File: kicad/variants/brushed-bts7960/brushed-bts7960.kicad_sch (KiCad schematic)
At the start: 57 parts, among them IC1 rp2040_RP2040_breakout_swd, J1 HDR-M-2.54_1x3, J2 HDR-M-2.54_1x4, J3 HDR-M-2.54_1x4, J4 HDR-M-2.54_1x4, U1 SN74AHC244DW, U2 BTN7970, U3 BTN7970, U4 BTN7970, U5 BTN7970, U6 BMI160, U7 SPX3819M5-L-3-3/TR

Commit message: feat(kicad): импорт платы из EasyEDA в KiCad
Завершает перенос варианта brushed-bts7960: схема уже была, плата
оставалась только в исходнике EasyEDA (easyeda/RP2040/PCB_RP2040.json).

Плату импортирует штатный конвертер KiCad (kicad-cli pcb import, формат
EasyEDA / JLCEDA Std) — свой парсер не пишем. Новый scripts/gen_pcb.py
поверх него доводит результат до вида репозитория:

- правила DRC из DRCRULE исходника (зазор 0.152 мм, дорожка 0.254 мм,
  via 0.61/0.305 мм, отдельный класс 5v) — иначе плата остаётся с
  дефолтами KiCad, под которые она не разводилась;
- перезаливка полигонов штатным ZONE_FILLER: импортёр переносит контуры
  COPPERAREA без вырезов под чужие цепи (~900 ложных нарушений DRC);
- выгрузка 14 футпринтов в kicad/common/footprints/biba.pretty/,
  канонические имена слоёв вместо EasyEDA-псевдонимов;
- 425 свободных падов и отверстий помечены board-only.

Схема и плата связаны: easyeda_sch2kicad.py проставляет Footprint,
имена у обоих генераторов из общей easyeda_netlist.footprint_name().

Проверено: связность совпадает с исходником побитово (56 сетей,
220 пин-назначений), 0 неразведённых пар, гербера и сверловка
экспортируются. DRC 1501 -> 555, остаток — свойства исходника
(массивы via в courtyard, шелкография, пады 0805/0603 без паяльной
пасты), разобран в README варианта.

gen_schematic.py помечен устаревшим (его вытеснил easyeda_sch2kicad.py)
и больше не затирает fp-lib-table и .kicad_pro.

Co-Authored-By: Claude Opus 5 <noreply@anthropic.com>
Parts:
- C1, C2, C3, C4, C5, C6: footprint (none) -> biba:C0805
- C7, C8: footprint (none) -> biba:C0603
- C9: footprint (none) -> biba:CAP-TH_BD16.0-P7.50-D0.8-FD-H25.0
- H1, H10, H2, H3, H4, H5, H6, H7, H8: footprint (none) -> biba:HDR-F-2.54_1X3
- IC1: footprint (none) -> biba:RP2040-BREAKOUT_SWD
- J1: footprint (none) -> biba:HDR-M-2.54_1X3
- J2, J3, J4: footprint (none) -> biba:HDR-M-2.54_1X4
- PM1: footprint (none) -> biba:SKMW30G-05
- R1, R10, R11, R12, R13, R14, R15, R16, R17, R18, R19, R2, R20, R25, R26, R3, R4, R5, R6, R7, R8, R9: footprint (none) -> biba:R0805
- R21, R22, R23, R24: footprint (none) -> biba:R0603
- U1: footprint (none) -> biba:SOIC-20_L12.8-W7.5-P1.27-LS10.3-BL
- U2, U3, U4, U5: footprint (none) -> biba:TO-263-7_L10.2-W10.4-P1.27-LS14.4-B
- U6: footprint (none) -> biba:LGA-14_L3.0-W2.5-P0.50-BL
- U7: footprint (none) -> biba:SOT-23-5_L3.0-W1.7-P0.95-LS2.8-BR

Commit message: feat(kicad): снабберы, супрессоры и керамика по питанию драйверов
Доработка по analysis/M1-driver-failure.md §5 — то, чего на плате не
хватало и что разбиралось при отказе нижнего ключа U2.

Добавлено в схему (11 позиций, стало 68 компонентов / 58 цепей):

- C10-C13 470 нФ X7R 50 В — керамика VS-GND у каждого драйвера U2-U5
  (§5.1); раньше её не было ни у одного.
- C14 1000 мкФ 50 В low-ESR — DC-link у пары U2/U3 (§5.2); единственный
  C9 стоит у U5, до U2/U3 по шине VIN 50-80 мм.
- R27+C15, R28+C16 — RC-снабберы 22 Ом 5 Вт + 100 нФ 100 В плёнка между
  выходами каждого моста, M1+/M1- и M2+/M2- (§5.7). 22 Ом — верх
  диапазона 10-22 Ом; рассеивание P=C*V^2*f ~1.3-2.5 Вт от R не зависит,
  а пиковый ток на фронте 1.1 А против 2.5 А при 10 Ом.
- D1, D2 1.5KE30CA — двунаправленные супрессоры на выводах моторов,
  параллельно снабберам. У 1.5KE30CA VC=41.4 В при 36 А, ниже
  абсолютного максимума VS=45 В у BTN7970.

Шина VIN осталась без супрессора: §5.3 анализа и статья держат TVS
именно там. Закрывается третьим корпусом D3 на VIN-GND у клеммы.

Заведён символ biba:TVS_BIDIR; футпринты выводных деталей — из
стандартных библиотек KiCad, резолвятся через глобальную fp-lib-table.

Метка цепи Vin -> VIN: имена сетей в KiCad регистрозависимы, на плате и
во всей документации цепь называется VIN.

Оба конвертера EasyEDA теперь отказываются затирать существующие
.kicad_sch/.kicad_pcb без --force: импорт разовый, дальше проект
ведётся в KiCad.

ERC без новых замечаний (остаются 2 исходные power_pin_not_driven).
На плату не перенесено.

Co-Authored-By: Claude Opus 5 <noreply@anthropic.com>
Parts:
- added C10, C11, C12, C13: 470n, biba:C0805, symbol biba:C
- added C14: 1000u, biba:CAP-TH_BD16.0-P7.50-D0.8-FD-H25.0, symbol biba:C_Pol
- added C15, C16: 100n 100V, Capacitor_THT:C_Rect_L10.0mm_W5.0mm_P5.00mm_P7.50mm, symbol biba:C
- added D1, D2: 1.5KE30CA, Diode_THT:D_DO-201AE_P15.24mm_Horizontal, symbol biba:TVS_BIDIR
- added R27, R28: 22R 5W, Resistor_THT:R_Axial_Power_L25.0mm_W9.0mm_P30.48mm, symbol biba:R
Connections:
- net GND: now also C10.2, C11.2, C12.2, C13.2, C14.2
- net M1+: now also D1.1 (A1), R27.1
- net M1-: now also C15.2, D1.2 (A2)
- net M2+: now also D2.1 (A1), R28.1
- net M2-: now also C16.2, D2.2 (A2)
- net Vin renamed VIN
- net VIN: now also C10.1, C11.1, C12.1, C13.1, C14.1
- new net M1_SNUB: C15.1, R27.2
- new net M2_SNUB: C16.1, R28.2
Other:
- note added: "50V low-ESR, у пары U2/U3"
- note added: "X7R 50V, VS-GND у U2"
- note added: "X7R 50V, VS-GND у U3"
- note added: "X7R 50V, VS-GND у U4"
- note added: "X7R 50V, VS-GND у U5"
- note added: "Доработка по analysis/M1-driver-failure.md §5 (керамика VS-GND, DC-link, TVS, снабберы)"
- note added: "Керамика VS-GND у каждого драйвера и DC-link по питанию"
- note added: "Снабберы RC и супрессоры на выводах моторов (R подбирается 10-22 Ом по осциллограмме OUT1-OUT2)"

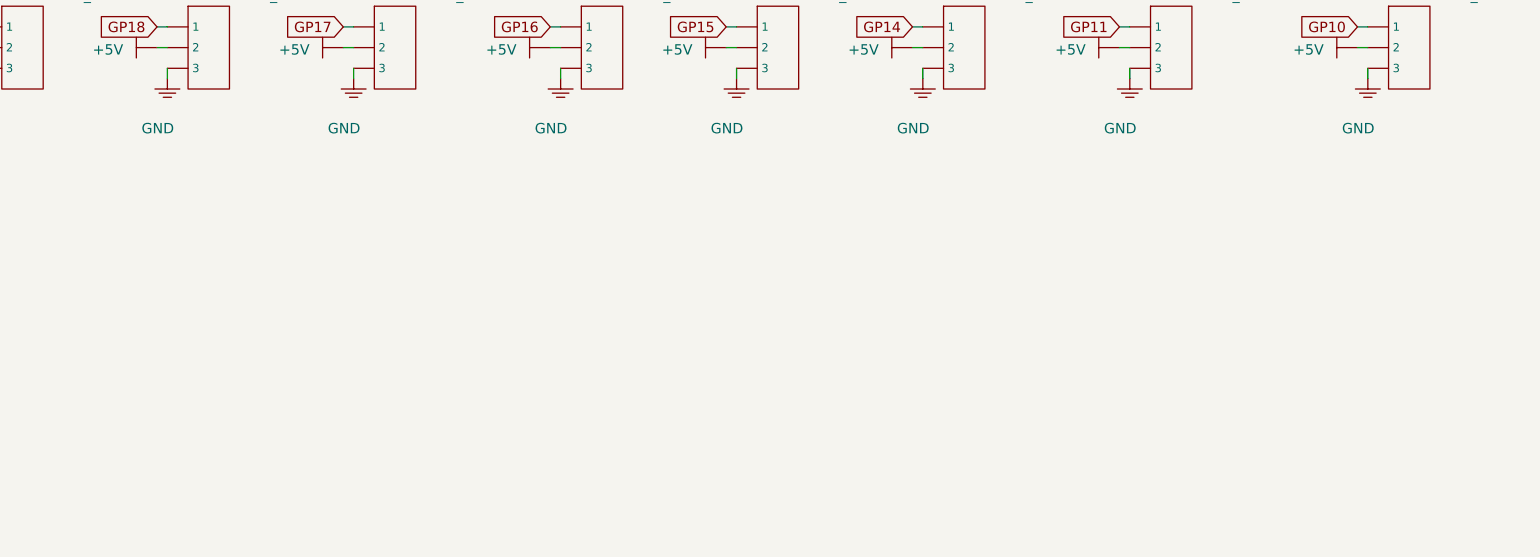
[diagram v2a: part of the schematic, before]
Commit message: feat(kicad): доработка на плате, расширение до 180x100, альтернативный DC/DC
Перенос доработки из схемы на плату + PM2.

Плата выросла 124.51x100.33 -> 180.51x100.33 мм (+56 мм вправо).
Причина: снабберные резисторы 5 Вт выводные, шаг 30.5 мм, корпус 25x9 мм.
На старую плату они не помещались нигде — ближайшее свободное место было
в 48 мм от клемм мотора, что смысл снаббера убивает.

В новой полосе справа от клемм:

- M1: D1 вертикально у клемм, R27 вправо, C15 обратно влево (y 55..76);
- M2: то же для D2/R28/C16 (y 88..109);
- PM2 внизу (y 117..138).

Шины M+ и M- идут параллельно и не пересекаются: клемма -> супрессор ->
резистор -> плёнка -> обратно понизу к клемме.

На старой части платы: C10-C13 470 нФ слева от выводов драйверов (под
корпусом TO-263 места нет), пад GND заведён переходным на нижний полигон;
C14 1000 мкФ вверху, симметрично C9 — как на доработанной вручную плате.

PM2 — Mean Well NSD10-48S5 (22-72 В -> 5 В / 2 А), альтернатива PM1
SKMW30G-05, ставится один из двух. Отверстия свои, не общие с PM1:
геометрия падов совпадает (DIP-6, ряды 20.32 мм), но назначение выводов
расходится — у SKMW30G на выводе 3 плюс выхода, у NSD10 минус выхода, на
выводе 4 у одного TRIM, у другого плюс. Общая разводка закоротила бы
выход NSD10. Каждый модуль разведён по своему даташиту. Футпринт
Converter_DCDC_MeanWell_NSD10_THT из стандартной библиотеки KiCad.

Схема и плата сходятся: 69 компонентов с обеих сторон, все 58 цепей
совпадают по составу пинов. DRC без новых ошибок зазоров, замыканий и
пересечений — остаток тот же, что был после импорта (переходные массивы
в courtyard драйверов, шелкография EasyEDA, пады 0805/0603 без пасты).

Не разведено, 6 связей: VIN у C10-C12 (прямая трасса к выводу 7 режет
веер сигнальных выводов 2-6, нужен обход низом), +5V и SW у PM2,
островок GND у вывода 1 U4.

Co-Authored-By: Claude Opus 5 <noreply@anthropic.com>
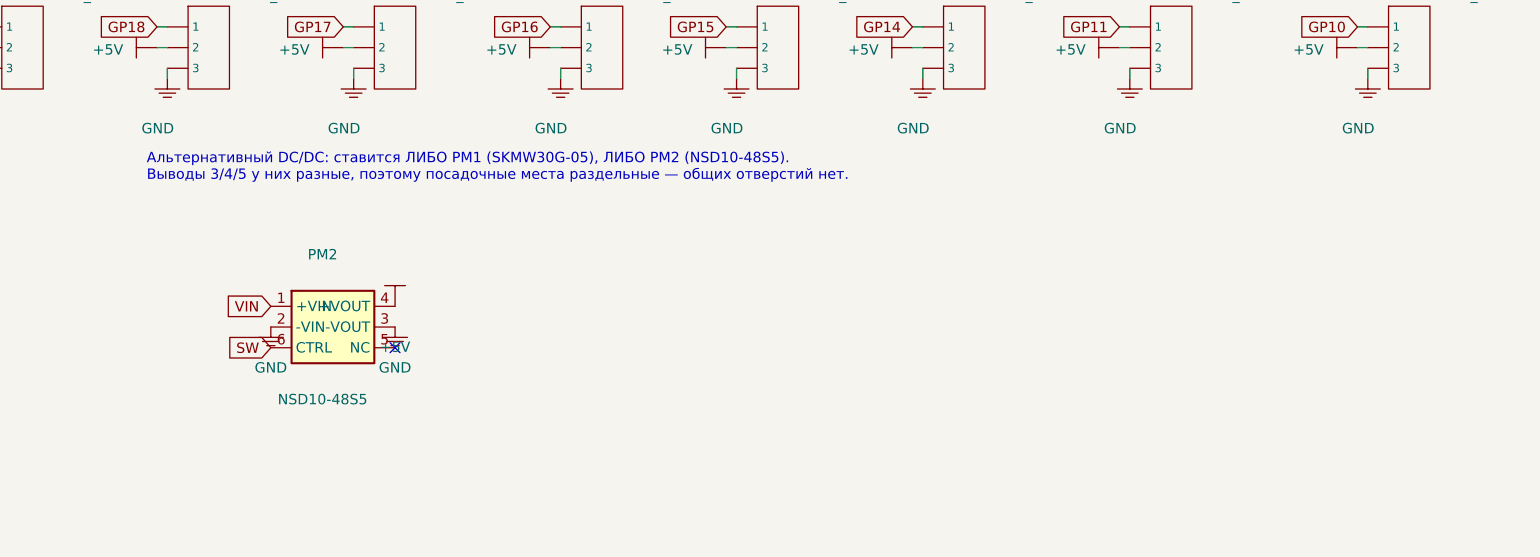
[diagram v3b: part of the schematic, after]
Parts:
- added PM2: NSD10-48S5, Converter_DCDC:Converter_DCDC_MeanWell_NSD10_THT, symbol biba:NSD10
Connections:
- net +5V: now also PM2.4 (+VOUT)
- net GND: now also PM2.2 (-VIN), PM2.3 (-VOUT)
- net SW: now also PM2.6 (CTRL)
- net VIN: now also PM2.1 (+VIN)
- no-connect marks 13 -> 14
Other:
- note added: "Альтернативный DC/DC: ставится ЛИБО PM1 (SKMW30G-05), ЛИБО PM2 (NSD10-48S5). Выводы 3/4/5 у них разные, поэтому посадочные места раздельные — общих отверстий нет."
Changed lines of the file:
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@@
       (effects (font (size 1.27 1.27)) hide))
   )
+  (text "Альтернативный DC/DC: ставится ЛИБО PM1 (SKMW30G-05), ЛИБО PM2 (NSD10-48S5).\nВыводы 3/4/5 у них разные, поэтому посадочные места раздельные — общих отверстий нет."
+    (at 227.33 227.33 0)
+    (effects (font (size 1.27 1.27)) (justify left bottom))
+)
+  (symbol (lib_id "biba:NSD10") (at 250.19 245.11 0) (unit 1)
+    (exclude_from_sim no) (in_bom yes) (on_board yes) (dnp no)
+    (property "Reference" "PM2" (at 248.92 236.22 0)
+      (effects (font (size 1.27 1.27))))
+    (property "Value" "NSD10-48S5" (at 248.92 254.00 0)
+      (effects (font (size 1.27 1.27))))
+    (property "Footprint" "Converter_DCDC:Converter_DCDC_MeanWell_NSD10_THT" (at 250.19 245.11 0)
+      (effects (font (size 1.27 1.27)) hide))
+    (property "Datasheet" "https://www.meanwell.com/Upload/PDF/NSD10-S/NSD10-S-SPEC.PDF" (at 250.19 245.11 0)
+      (effects (font (size 1.27 1.27)) hide))
+    (property "Package" "" (at 250.19 245.11 0) (effects (font (size 1.27 1.27)) hide))
+    (property "LCSC" "" (at 250.19 245.11 0) (effects (font (size 1.27 1.27)) hide))
+    (property "MPN" "NSD10-48S5" (at 250.19 245.11 0) (effects (font (size 1.27 1.27)) hide))
+    (pin "1")
+    (pin "2")
+    (pin "6")
+    (pin "4")
+    (pin "3")
+    (pin "5")
+    (instances (project "brushed-bts7960" (path "/5d1025ef-bd26-5426-bb12-5355817dfc1c" (reference "PM2") (unit 1))))
+  )
+  (global_label "VIN" (shape input) (at 242.57 242.57 180)
+    (fields_autoplaced yes)
+    (effects (font (size 1.27 1.27)) (justify right))
+    (property "Intersheetrefs" "${INTERSHEET_REFS}" (at 242.57 242.57 0)
+      (effects (font (size 1.27 1.27)) hide))
+  )
+  (symbol (lib_id "biba:GND") (at 242.57 245.11 0) (unit 1)
+    (exclude_from_sim no) (in_bom no) (on_board no) (dnp no)
+    (property "Reference" "#PWR120" (at 242.57 245.11 0) (effects (font (size 1.27 1.27)) hide))
+    (property "Value" "GND" (at 242.57 250.11 0)
+      (effects (font (size 1.27 1.27))))
+    (property "Footprint" "" (at 242.57 245.11 0) (effects (font (size 1.27 1.27)) hide))
+    (property "Datasheet" "" (at 242.57 245.11 0) (effects (font (size 1.27 1.27)) hide))
+    (pin "1")
+    (instances (project "brushed-bts7960" (path "/5d1025ef-bd26-5426-bb12-5355817dfc1c" (reference "#PWR120") (unit 1))))
+  )
+  (global_label "SW" (shape input) (at 242.57 247.65 180)
+    (fields_autoplaced yes)
+    (effects (font (size 1.27 1.27)) (justify right))
+    (property "Intersheetrefs" "${INTERSHEET_REFS}" (at 242.57 247.65 0)
+      (effects (font (size 1.27 1.27)) hide))
+  )
+  (symbol (lib_id "biba:+5V") (at 257.81 242.57 0) (unit 1)
+    (exclude_from_sim no) (in_bom no) (on_board no) (dnp no)
+    (property "Reference" "#PWR121" (at 257.81 242.57 0) (effects (font (size 1.27 1.27)) hide))
+    (property "Value" "+5V" (at 257.81 247.57 0)
+      (effects (font (size 1.27 1.27))))
+    (property "Footprint" "" (at 257.81 242.57 0) (effects (font (size 1.27 1.27)) hide))
+    (property "Datasheet" "" (at 257.81 242.57 0) (effects (font (size 1.27 1.27)) hide))
+    (pin "1")
+    (instances (project "brushed-bts7960" (path "/5d1025ef-bd26-5426-bb12-5355817dfc1c" (reference "#PWR121") (unit 1))))
+  )
+  (symbol (lib_id "biba:GND") (at 257.81 245.11 0) (unit 1)
+    (exclude_from_sim no) (in_bom no) (on_board no) (dnp no)
+    (property "Reference" "#PWR122" (at 257.81 245.11 0) (effects (font (size 1.27 1.27)) hide))
+    (property "Value" "GND" (at 257.81 250.11 0)
+      (effects (font (size 1.27 1.27))))
+    (property "Footprint" "" (at 257.81 245.11 0) (effects (font (size 1.27 1.27)) hide))
+    (property "Datasheet" "" (at 257.81 245.11 0) (effects (font (size 1.27 1.27)) hide))
+    (pin "1")
+    (instances (project "brushed-bts7960" (path "/5d1025ef-bd26-5426-bb12-5355817dfc1c" (reference "#PWR122") (unit 1))))
+  )
+  (no_connect (at 257.81 247.65))
   (sheet_instances
     (path "/" (page "1"))
